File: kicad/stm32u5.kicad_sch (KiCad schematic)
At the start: 10 parts, among them SW5 BOOTSEL, U12 STM32U535CET6-modified

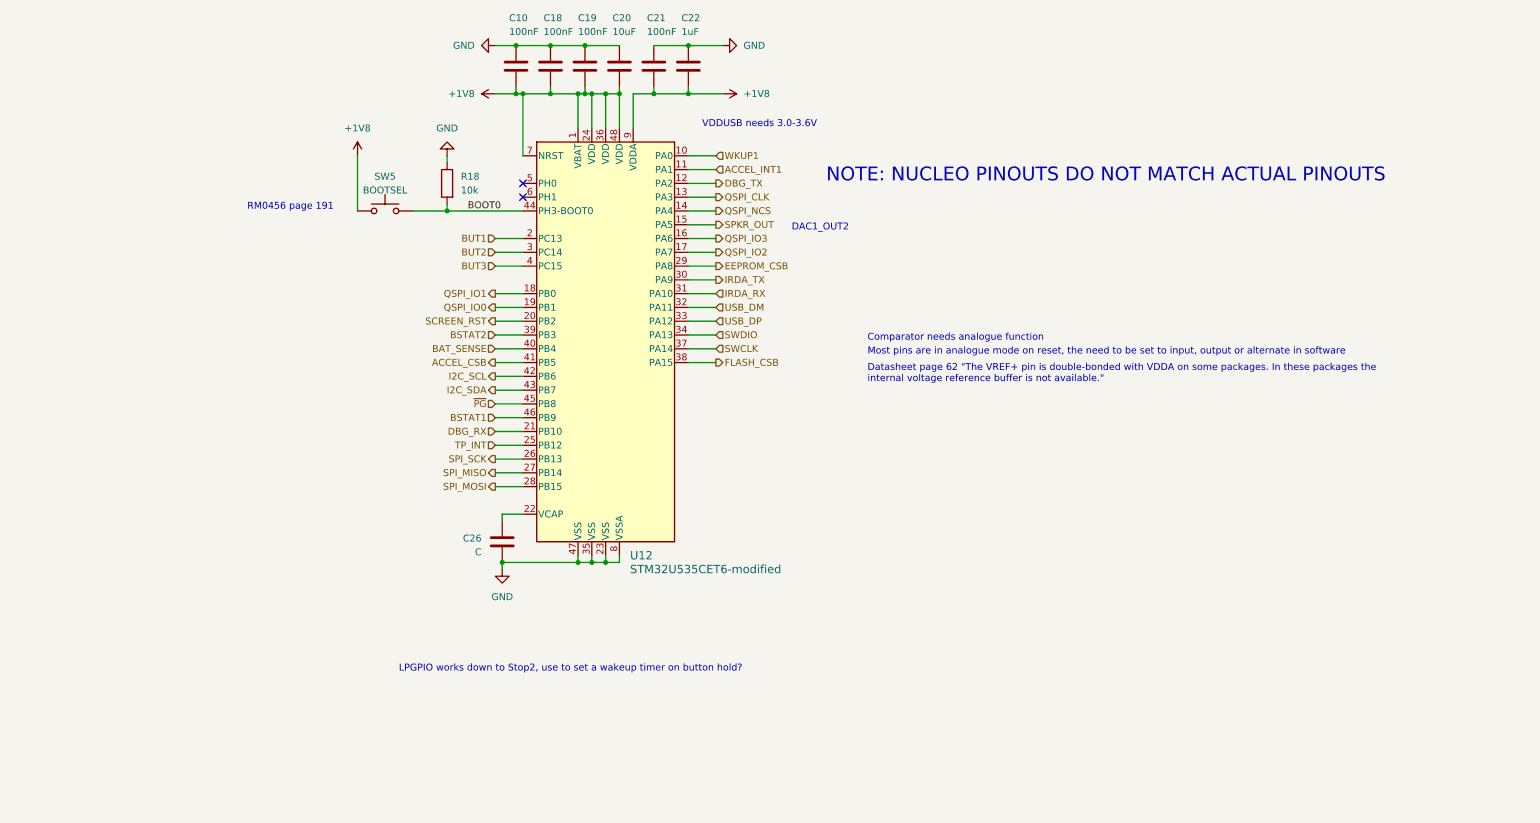
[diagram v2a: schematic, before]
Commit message: comments about power, changed eeprom and flash packages
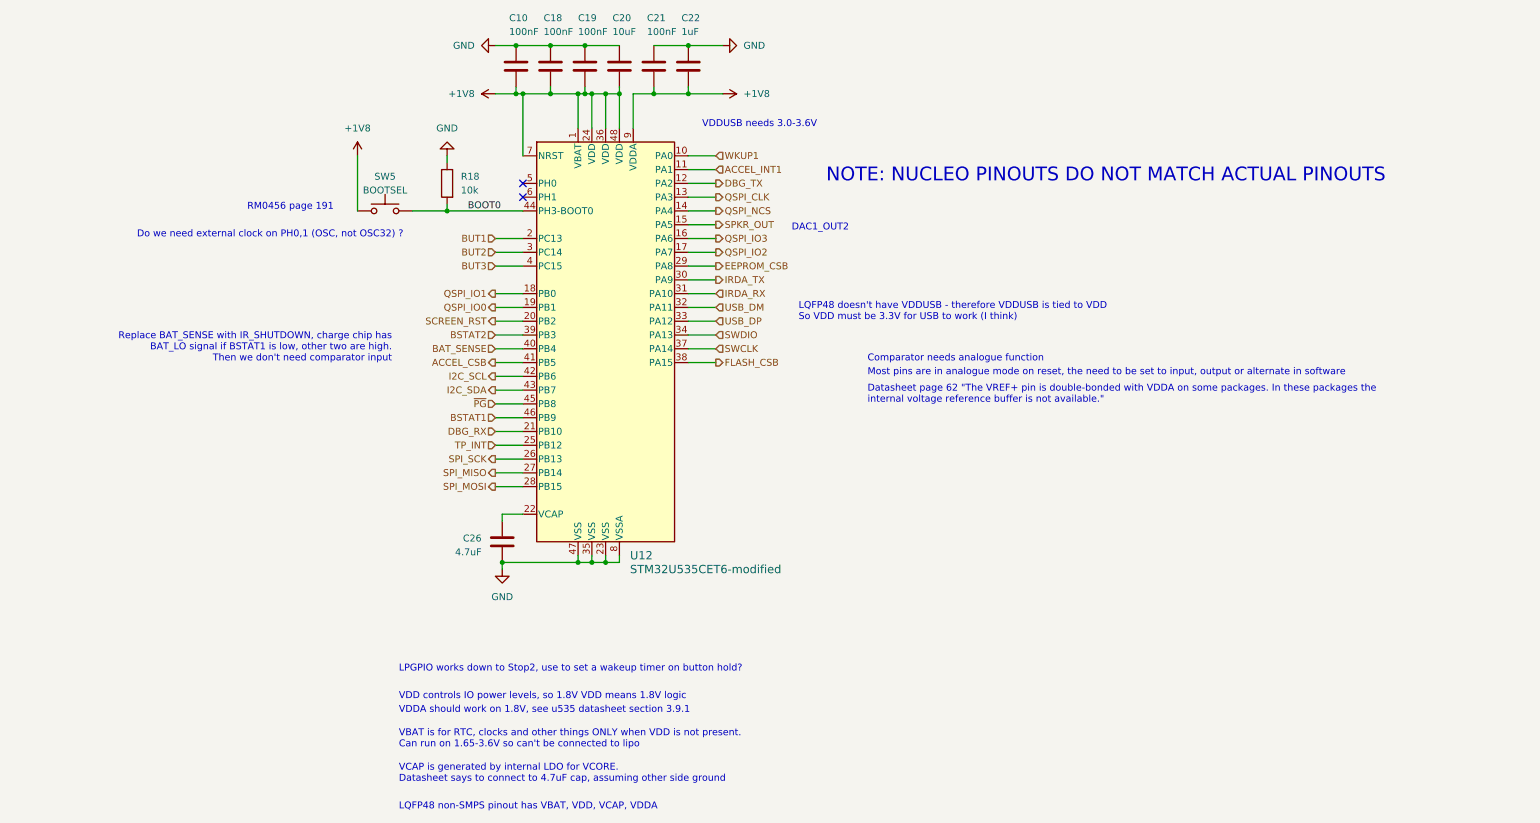
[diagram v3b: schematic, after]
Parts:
- C26: value C -> 4.7uF
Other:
- note added: "Do we need external clock on PH0,1 (OSC, not OSC32) ?"
- note added: "LQFP48 doesn't have VDDUSB - therefore VDDUSB is tied to VDD So VDD must be 3.3V for USB to work (I think)"
- note added: "LQFP48 non-SMPS pinout has VBAT, VDD, VCAP, VDDA"
- note added: "Replace BAT_SENSE with IR_SHUTDOWN, charge chip has BAT_LO signal if BSTAT1 is low, other two are high. Then we don't need comparator input"
- note added: "VBAT is for RTC, clocks and other things ONLY when VDD is not present. Can run on 1.65-3.6V so can't be connected to lipo"
- note added: "VCAP is generated by internal LDO for VCORE. Datasheet says to connect to 4.7uF cap, assuming other side ground"
- note added: "VDD controls IO power levels, so 1.8V VDD means 1.8V logic"
- note added: "VDDA should work on 1.8V, see u535 datasheet section 3.9.1"
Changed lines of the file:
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@@
     (stroke (width 0) (type default))
+  )
+  (text "VBAT is for RTC, clocks and other things ONLY when VDD is not present.\nCan run on 1.65-3.6V so can't be connected to lipo"
+    (at 77.47 153.67 0)
+    (effects (font (size 1.27 1.27)) (justify left bottom))
   )
   (text "LPGPIO works down to Stop2, use to set a wakeup timer on button hold?"
@@
     (effects (font (size 1.27 1.27)) (justify left bottom))
   )
+  (text "Replace BAT_SENSE with IR_SHUTDOWN, charge chip has \nBAT_LO signal if BSTAT1 is low, other two are high.\nThen we don't need comparator input"
+    (at 76.2 82.55 0)
+    (effects (font (size 1.27 1.27)) (justify right bottom))
+  )
   (text "DAC1_OUT2" (at 149.86 58.42 0)
+    (effects (font (size 1.27 1.27)) (justify left bottom))
+  )
+  (text "Do we need external clock on PH0,1 (OSC, not OSC32) ?"
+    (at 29.21 59.69 0)
+    (effects (font (size 1.27 1.27)) (justify left bottom))
+  )
+  (text "LQFP48 doesn't have VDDUSB - therefore VDDUSB is tied to VDD\nSo VDD must be 3.3V for USB to work (I think)"
+    (at 151.13 74.93 0)
     (effects (font (size 1.27 1.27)) (justify left bottom))
   )
@@
     (effects (font (size 2.54 2.54) (color 255 9 0 1)) (justify left bottom))
   )
+  (text "LQFP48 non-SMPS pinout has VBAT, VDD, VCAP, VDDA" (at 77.47 165.1 0)
+    (effects (font (size 1.27 1.27)) (justify left bottom))
+  )
   (text "RM0456 page 191" (at 49.53 54.61 0)
     (effects (font (size 1.27 1.27)) (justify left bottom))
   )
+  (text "VCAP is generated by internal LDO for VCORE.\nDatasheet says to connect to 4.7uF cap, assuming other side ground"
+    (at 77.47 160.02 0)
+    (effects (font (size 1.27 1.27)) (justify left bottom))
+  )
   (text "Datasheet page 62 \"The VREF+ pin is double-bonded with VDDA on some packages. In these packages the\ninternal voltage reference buffer is not available.\""
-    (at 163.83 86.36 0)
-    (effects (font (size 1.27 1.27)) (justify left bottom))
-  )
-  (text "Comparator needs analogue function" (at 163.83 78.74 0)
+    (at 163.83 90.17 0)
+    (effects (font (size 1.27 1.27)) (justify left bottom))
+  )
+  (text "VDDA should work on 1.8V, see u535 datasheet section 3.9.1"
+    (at 77.47 147.32 0)
+    (effects (font (size 1.27 1.27)) (justify left bottom))
+  )
+  (text "Comparator needs analogue function" (at 163.83 82.55 0)
     (effects (font (size 1.27 1.27)) (justify left bottom))
   )
@@
   )
   (text "Most pins are in analogue mode on reset, the need to be set to input, output or alternate in software"
-    (at 163.83 81.28 0)
+    (at 163.83 85.09 0)
+    (effects (font (size 1.27 1.27)) (justify left bottom))
+  )
+  (text "VDD controls IO power levels, so 1.8V VDD means 1.8V logic"
+    (at 77.47 144.78 0)
     (effects (font (size 1.27 1.27)) (justify left bottom))
   )
@@
       (effects (font (size 1.27 1.27)) (justify right))
     )
-    (property "Value" "C" (at 92.71 117.475 0)
+    (property "Value" "4.7uF" (at 92.71 117.475 0)
       (effects (font (size 1.27 1.27)) (justify right))
     )
